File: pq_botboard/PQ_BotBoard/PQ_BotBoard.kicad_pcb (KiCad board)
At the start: 4 copper layers, 64 x 52 mm, 15 parts, among them CN1 CONN-SMD_532610271, CN2 REF, CN3 MOLEX 0533980667, IC1 TCN75AVUA713-VAO

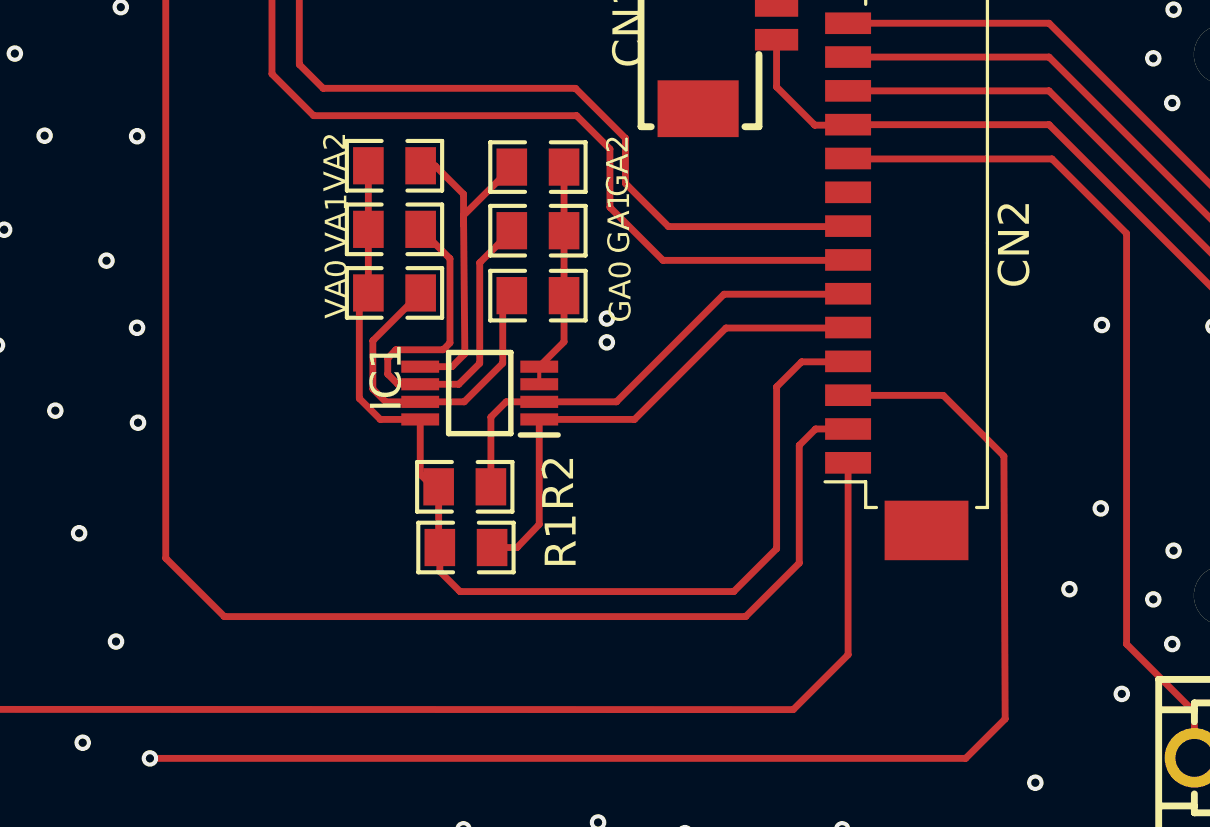
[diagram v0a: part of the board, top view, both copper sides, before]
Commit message: killswitch and batt- pins swapped
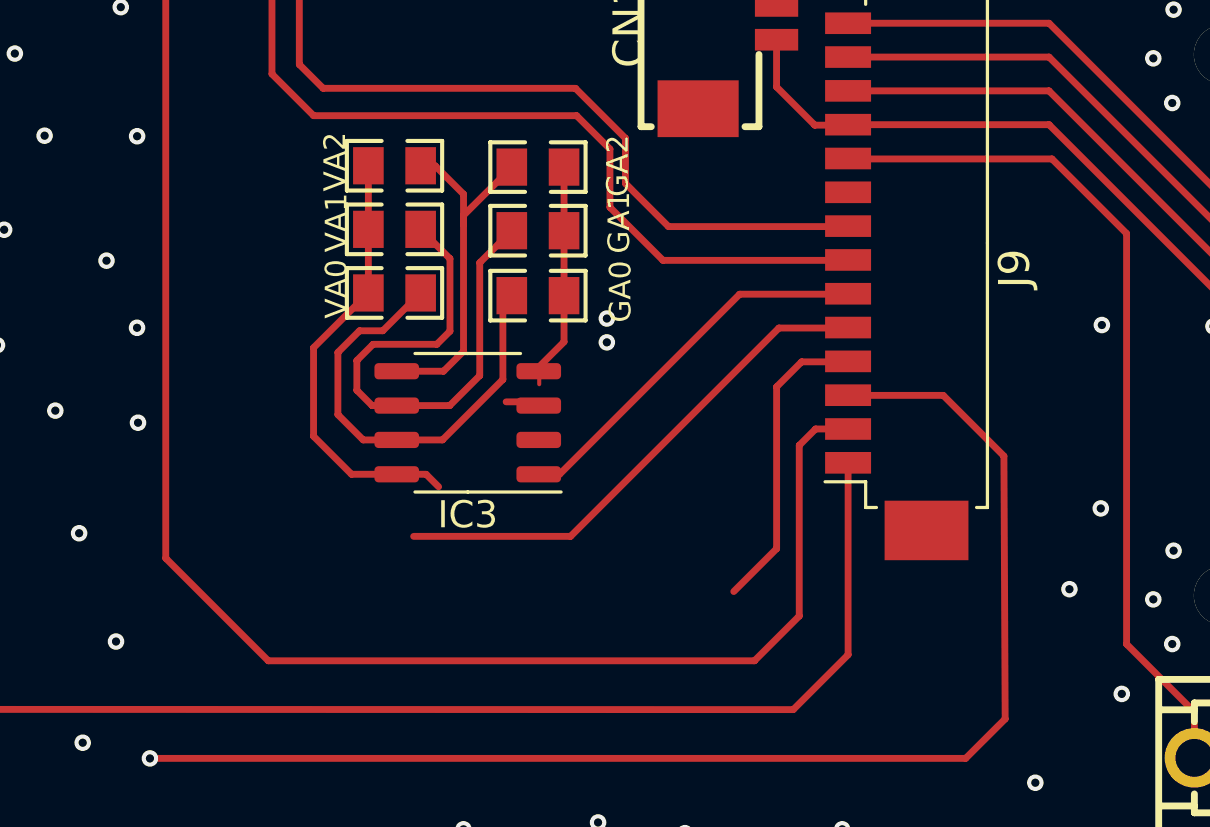
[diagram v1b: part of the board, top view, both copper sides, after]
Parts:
- removed IC1: TCN75AVUA713-VAO, easyeda:SOP65P490X110-8N
- removed R1, R2: 5k, easyeda:R0805
- added IC3: TCN75AVUA713, Package_SO:SOP-8_3.9x4.9mm_P1.27mm, F.Cu at (95.1, 60.6)
- J5: renamed from CN3; value MOLEX 0533980667 -> 533980671
- J9: renamed from CN2; value REF -> 53261-1471
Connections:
- D8 pad 1: (no net) -> Net-(D8-Pad1)
- D8 pad 2: (no net) -> Net-(D8-Pad2)
- GA0 pad 1: (no net) -> /GND
- GA0 pad 2: (no net) -> Net-(GA0-Pad2)
- GA1 pad 1: (no net) -> /GND
- GA1 pad 2: (no net) -> Net-(GA1-Pad2)
- GA2 pad 1: (no net) -> /GND
- GA2 pad 2: (no net) -> Net-(GA2-Pad2)
- J5 pad 1: (no net) -> /BATT-
- J5 pad 2: (no net) -> /BATT+
- J5 pad 3: (no net) -> /NRST
- J5 pad 4: (no net) -> /SWCLK
- J5 pad 5: (no net) -> /SWDIO
- J5 pad 6: (no net) -> /VCC_Umbilical
- J9 pad 1: (no net) -> /SOLAR_Y
- J9 pad 10: (no net) -> /BATT-
- J9 pad 11: (no net) -> /KILLSWITCH+
- J9 pad 12: (no net) -> /NRST
- J9 pad 13: (no net) -> /SWCLK
- J9 pad 14: (no net) -> /SWDIO
- J9 pad 2: (no net) -> /GND
- J9 pad 3: (no net) -> /MAG-Y
- J9 pad 4: (no net) -> /ADCS_POWER
- J9 pad 5: (no net) -> /VCC
- J9 pad 6: (no net) -> /SDA
- J9 pad 7: (no net) -> /SCL
- J9 pad 8: (no net) -> Net-(D8-Pad1)
- J9 pad 9: (no net) -> Net-(D8-Pad2)
- VA0 pad 1: (no net) -> Net-(GA0-Pad2)
- VA0 pad 2: (no net) -> /VCC
- VA1 pad 1: (no net) -> Net-(GA1-Pad2)
- VA1 pad 2: (no net) -> /VCC
- VA2 pad 1: (no net) -> Net-(GA2-Pad2)
- VA2 pad 2: (no net) -> /VCC
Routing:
- net (no net): track 15035.2 -> 32.0 mm, vias 156 -> 129
- net /MAG-Y: track 0.00 -> 14579.4 mm, vias 0 -> 19
- net /VCC_Umbilical: track 0.00 -> 44.5 mm, vias 0 -> 1
- net Net-(D8-Pad1): track 0.00 -> 42.9 mm, vias 0 -> 1
- net /SOLAR_Y: track 0.00 -> 41.8 mm, vias 0 -> 1
- net Net-(D8-Pad2): track 0.00 -> 39.1 mm, vias 0 -> 1
- net /VCC: track 0.00 -> 35.4 mm
- net /BATT-: track 0.00 -> 31.9 mm
- net /KILLSWITCH+: track 0.00 -> 28.5 mm, vias 0 -> 1
- net /SWCLK: track 0.00 -> 23.6 mm, vias 0 -> 1
- net /BATT+: track 0.00 -> 23.6 mm, vias 0 -> 1
- net /NRST: track 0.00 -> 23.6 mm, vias 0 -> 1
- net Net-(GA1-Pad2): track 0.00 -> 20.3 mm
- net Net-(GA0-Pad2): track 0.00 -> 16.9 mm
- net /SDA: track 0.00 -> 14.1 mm
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- added copper zone on F.Cu, net /GND
- removed copper zone on F.Cu, net (none)
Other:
- copper layers 4 -> 6

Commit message: files changed
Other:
- board text added: "Replace vias by holes MTQ shit in layers 3 and 4 Revise connectors pins in general"
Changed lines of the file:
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@@
   (gr_line (start 70.042 30.988) (end 134.042 30.988) (layer "Edge.Cuts") (width 0.254))
   (gr_line (start 70.042 82.989) (end 70.042 40.023) (layer "Edge.Cuts") (width 0.254))
+  (gr_text "Replace vias by holes\nMTQ shit in layers 3 and 4\nRevise connectors pins in general" (at 92.7 109.2) (layer "F.Cu")
+    (effects (font (size 1.5 1.5) (thickness 0.3)) (justify left))
+  )
   (gr_text "BOTTOM BOARD" (at 89.93 41.24) (layer "F.SilkS")
     (effects (font (size 2.032 2.032) (thickness 0.203)) (justify left))

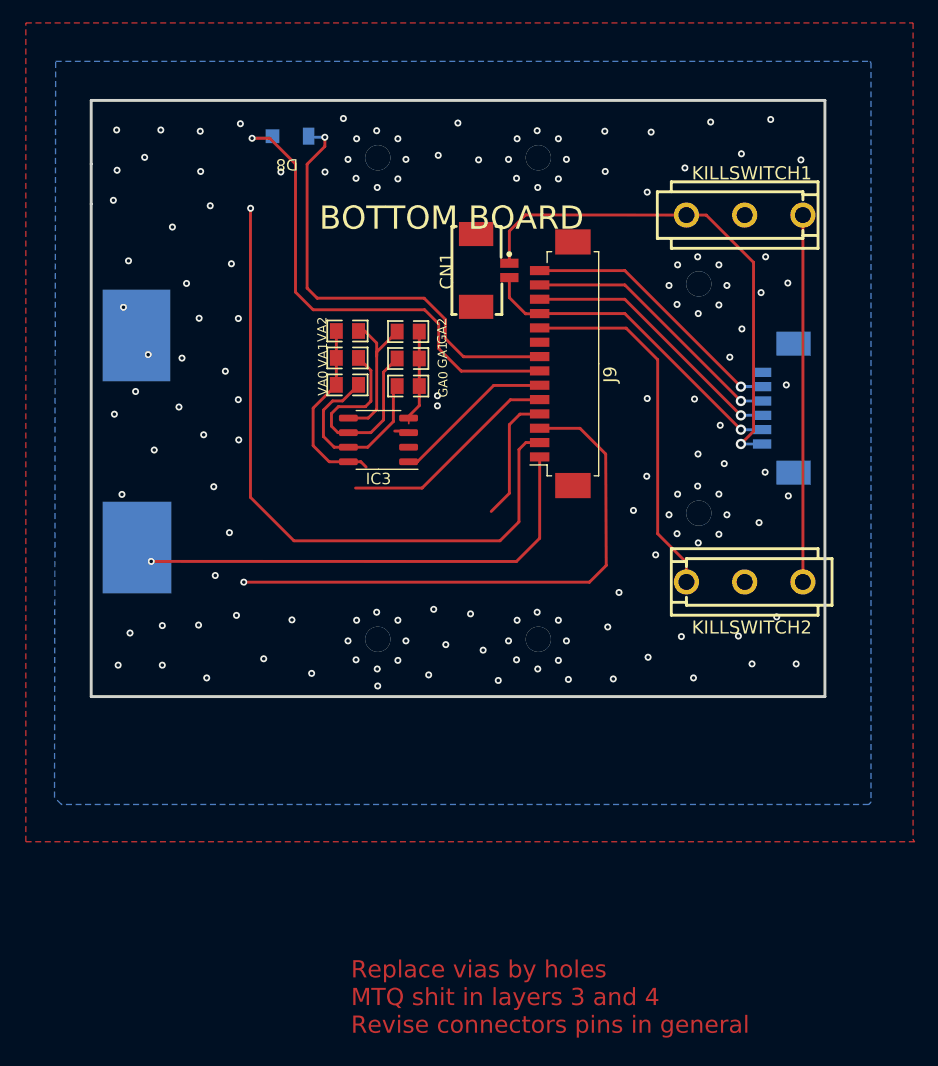
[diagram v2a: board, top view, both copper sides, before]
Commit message: Lateral, Bottom and MagY boards done
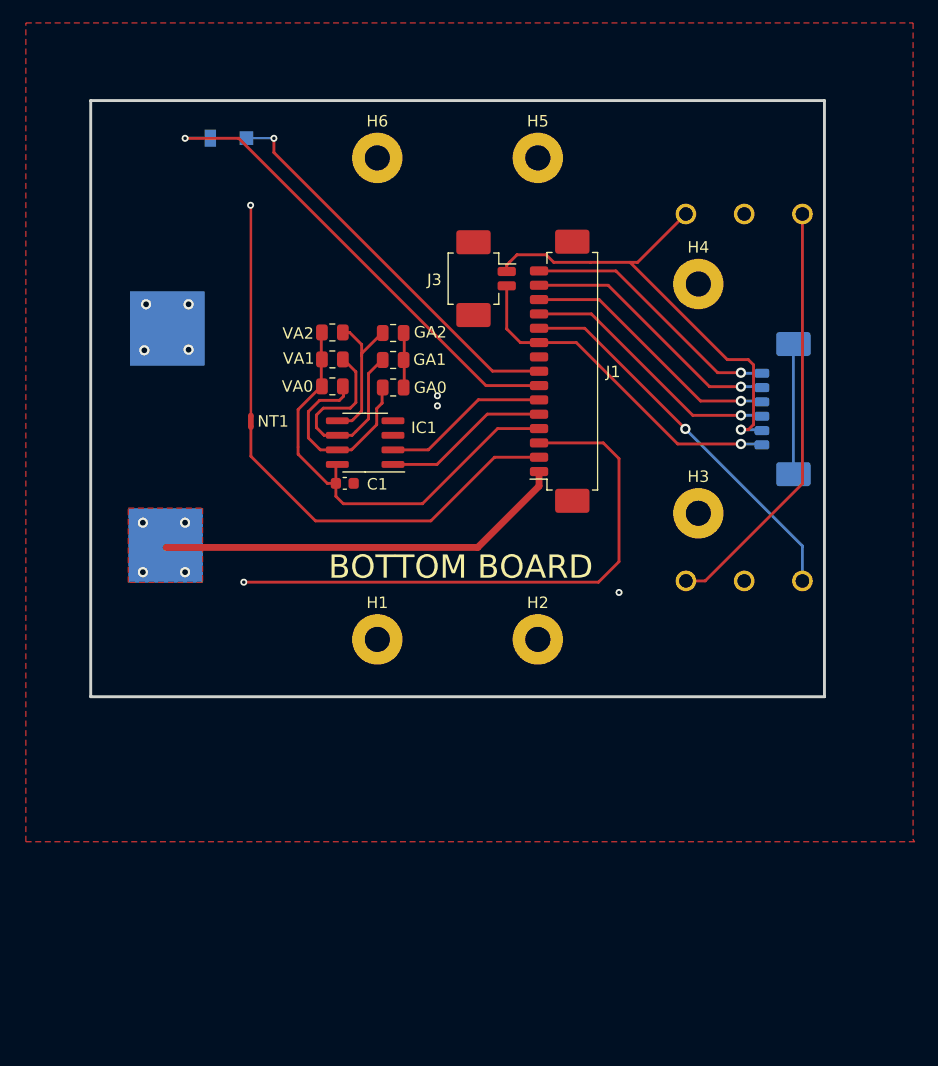
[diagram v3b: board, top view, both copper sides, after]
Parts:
- removed CN1: CONN-SMD_532610271, easyeda:CONN-SMD_532610271
- removed D8: SLCD-61N8, NSL_misc:SLCD-61N8
- removed IC3: TCN75AVUA713, Package_SO:SOP-8_3.9x4.9mm_P1.27mm
- removed J5: 533980671, easyeda:MOLEX 0533980667
- removed J9: 53261-1471, easyeda:MOLEX_PICOBLADE_53261-1471_14X1.25MM_ANGLED
- removed KILLSWITCH1, KILLSWITCH2: SW-TH_D2F-01L, easyeda:SW-TH_D2F-01L
- added C1: 1 uF, Capacitor_SMD:C_0603_1608Metric, F.Cu at (92.2, 64.4)
- added D1: D_Photo, NSL_misc:SLCD-61N8, B.Cu at (82.3, 34.4)
- added H1: MountingHole_Pad, MountingHole:MountingHole_2.2mm_M2_Pad, F.Cu at (95.0, 78.0)
- added H2: MountingHole_Pad, MountingHole:MountingHole_2.2mm_M2_Pad, F.Cu at (109.0, 78.0)
- added H3: MountingHole_Pad, MountingHole:MountingHole_2.2mm_M2_Pad, F.Cu at (123.0, 67.0)
- added H4: MountingHole_Pad, MountingHole:MountingHole_2.2mm_M2_Pad, F.Cu at (123.0, 47.0)
- added H5: MountingHole_Pad, MountingHole:MountingHole_2.2mm_M2_Pad, F.Cu at (109.0, 36.0)
- added H6: MountingHole_Pad, MountingHole:MountingHole_2.2mm_M2_Pad, F.Cu at (95.0, 36.0)
- added IC1: TCN75AVOA713, Package_SO:SOP-8_3.9x4.9mm_P1.27mm, F.Cu at (93.9, 60.8)
- added J1: 53261-1471, Connector_Molex:Molex_PicoBlade_53261-1571_1x15-1MP_P1.25mm_Horizontal, F.Cu at (111.5, 54.6)
- added J2: 533980671, Connector_Molex:Molex_PicoBlade_53398-0671_1x06-1MP_P1.25mm_Vertical, B.Cu at (129.8, 57.9)
- added J3: 53261-0271, Connector_Molex:Molex_PicoBlade_53261-0271_1x02-1MP_P1.25mm_Horizontal, F.Cu at (103.9, 46.5)
- added KS1: D2F-01L-A1, SamacSys_Parts:D2FLA1, B.Cu at (121.9, 40.9)
- added KS2: D2F-01L-A, SamacSys_Parts:D2FLA, B.Cu at (121.9, 72.9)
- added NT1: NetTie_2, NetTie:NetTie-2_SMD_Pad0.5mm, F.Cu at (84.0, 59.0)
- added S1: SolarCell, NSL_power:Solar_Cell, B.Cu at (99.5, 56.8)
- GA0, GA1, GA2, VA0, VA1, VA2: value 5k -> 0R; footprint easyeda:R0805 -> Resistor_SMD:R_0805_2012Metric
- moved GA1 1.32 mm to (96.4, 53.6)
- moved GA2 1.32 mm to (96.4, 51.3)
- moved VA2 1.32 mm to (91.1, 51.2)
- moved GA0 1.32 mm to (96.4, 56.0)
- moved VA0 1.32 mm to (91.1, 55.9)
- moved VA1 1.32 mm to (91.1, 53.6)
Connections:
- net /GND renamed GND
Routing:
- net /MAG-Y: track 14579.4 -> 32.3 mm, vias 19 -> 0
- net /VCC_MAG: track 0.00 -> 9704.1 mm, vias 0 -> 5
- net Net-(D8-Pad1): track 42.9 -> 0.00 mm, vias 1 -> 0
- net /PH-: track 0.00 -> 42.0 mm, vias 0 -> 1
- net Net-(D8-Pad2): track 39.1 -> 0.00 mm, vias 1 -> 0
- net Net-(KS1-Pad3): track 0.00 -> 37.2 mm
- net /PH+: track 0.00 -> 34.7 mm, vias 0 -> 1
- net (no net): track 32.0 -> 0.00 mm, vias 129 -> 0
- net /SWDIO: track 0.00 -> 23.1 mm, vias 0 -> 1
- net /VCC_Umbilical: track 44.5 -> 23.1 mm
- net /BATT+: track 23.6 -> 41.4 mm
- net /SCL: track 0.00 -> 14.6 mm
- net unconnected-(J2-PadMP): track 0.00 -> 11.4 mm
- net /ADCS_POWER: track 11.2 -> 0.00 mm
- net /SOLAR_Y: track 41.8 -> 36.0 mm, vias 1 -> 4
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- added copper zone on F.Cu, net /SOLAR_Y
- removed copper zone on B.Cu, net (none)
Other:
- outline, holes or cut-outs redrawn
- board text added: "+X"
- board text added: "+Z"
- board text added: "-X"
- board text added: "-Z"
- board text removed: "Replace vias by holes MTQ shit in layers 3 and 4 Revise connectors pins in general"

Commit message: Functional revision and finishing touches part I
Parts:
- removed S1: SolarCell, NSL_power:Solar_Cell
- added Annotation1: Silkscreen_Annotation, symbols-nsl:GRSS, B.Cu at (75.5, 60.2)
- added Annotation2: Silkscreen_Annotation, symbols-nsl:IEEE_logo, B.Cu at (75.5, 40.4)
- added Annotation3: Silkscreen_Annotation, symbols-nsl:UPC_positiu, B.Cu at (81.7, 78.5)
- added Annotation4: Silkscreen_Annotation, symbols-nsl:Telecos, B.Cu at (123.5, 57.1)
- added Annotation5: Silkscreen_Annotation, symbols-nsl:Bridgemaker, F.Cu at (101.1, 57.2)
- added SC1: Solar_Cell, power-nsl:Azur-Space-PQ-cut-SC, B.Cu at (99.5, 56.8)
- D1: value D_Photo -> SLCD-61N8; footprint NSL_misc:SLCD-61N8 -> passive-nsl:SLCD-61N8
- KS1: footprint SamacSys_Parts:D2FLA1 -> miscelaneous-nsl:D2FLA1
- KS2: footprint SamacSys_Parts:D2FLA -> miscelaneous-nsl:D2FLA
- moved D1 0.33 mm to (82.0, 34.2)
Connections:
- D1 pad 1: /PH- -> /PH+
- D1 pad 2: /PH+ -> /PH-

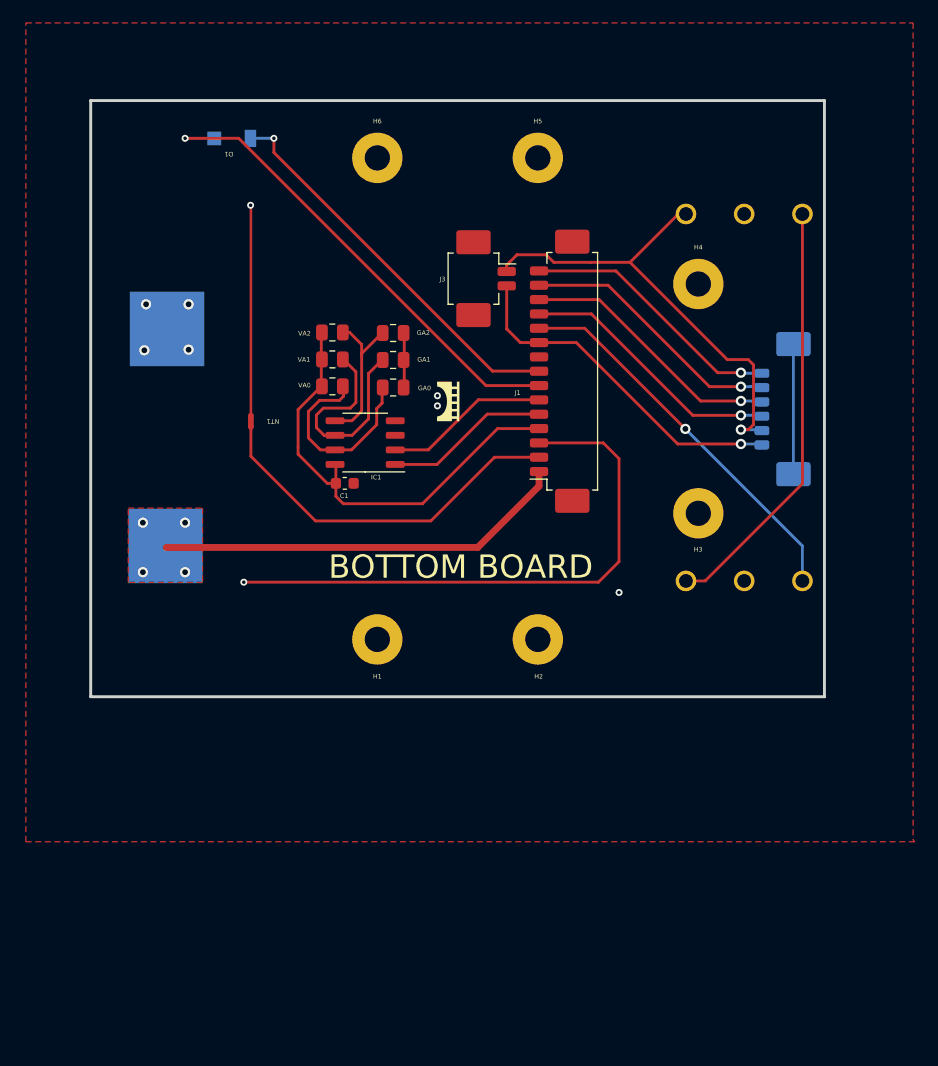
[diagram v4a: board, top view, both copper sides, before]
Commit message: Full Kicad7 transition, library improvement and adaptation, correct footprints and 3D models added
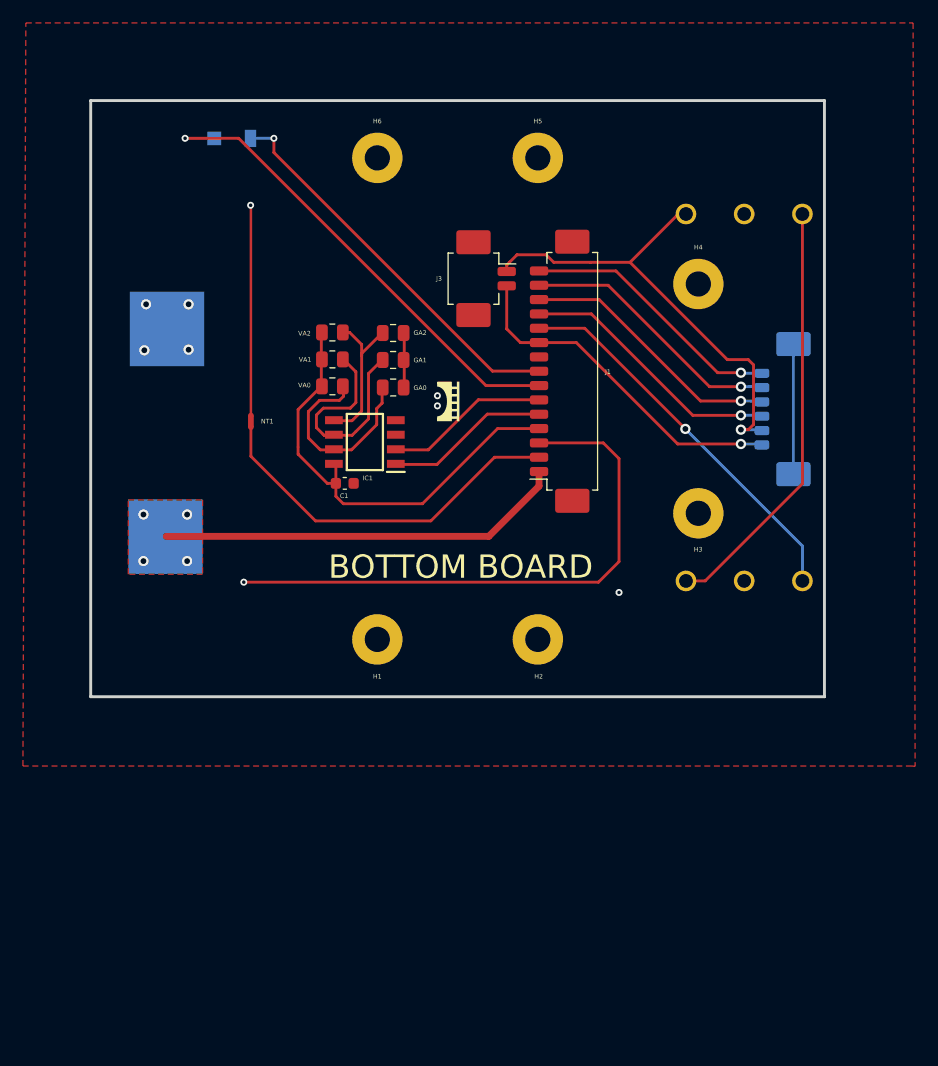
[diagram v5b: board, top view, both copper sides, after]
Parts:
- Annotation1: footprint symbols-nsl:GRSS -> -nsl_symbols:GRSS
- Annotation2: footprint symbols-nsl:IEEE_logo -> -nsl_symbols:IEEE_logo
- Annotation3: footprint symbols-nsl:UPC_positiu -> -nsl_symbols:UPC_positiu
- Annotation4: footprint symbols-nsl:Telecos -> -nsl_symbols:Telecos
- Annotation5: footprint symbols-nsl:Bridgemaker -> -nsl_symbols:Bridgemaker
- D1: footprint passive-nsl:SLCD-61N8 -> -nsl_passive:SLCD-61N8
- IC1: footprint Package_SO:SOP-8_3.9x4.9mm_P1.27mm -> -nsl_sensor:TCN75AVOA
- KS1: footprint miscelaneous-nsl:D2FLA1 -> -nsl_miscellaneous:D2FLA1
- KS2: footprint miscelaneous-nsl:D2FLA -> -nsl_miscellaneous:D2FLA
- SC1: footprint power-nsl:Azur-Space-PQ-cut-SC -> -nsl_power:Azur-Space-PQ-cut-SC

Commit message: fabrication
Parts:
- added NT2: NetTie_2, NetTie:NetTie-2_SMD_Pad0.5mm, F.Cu at (106.8, 55.9)
- J2: value 533980671 -> Conn_01x08_MountingPin; footprint Connector_Molex:Molex_PicoBlade_53398-0671_1x06-1MP_P1.25mm_Vertical -> Connector_Molex:Molex_PicoBlade_53398-0871_1x08-1MP_P1.25mm_Vertical
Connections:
- J1 pad 7: /PH- -> GND
- J1 pad 9: GND -> /SWO
- J2 pad 4: /NRST -> /SWO
- J2 pad 5: /BATT+ -> /NRST
- J2 pad 6: /BATT- -> /BATT+
- J2 pad MP: unconnected-(J2-MountPin-PadMP) -> GND
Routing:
- net /SWO: track 0.00 -> 29.1 mm, vias 0 -> 1
- net unconnected-(J2-MountPin-PadMP): track 11.4 -> 0.00 mm
- net /PH-: track 42.4 -> 39.6 mm
- net /BATT+: track 41.4 -> 44.2 mm
- net GND: track 4.75 -> 4.82 mm, vias 4 -> 8
- added copper zone on B.Cu, net GND
